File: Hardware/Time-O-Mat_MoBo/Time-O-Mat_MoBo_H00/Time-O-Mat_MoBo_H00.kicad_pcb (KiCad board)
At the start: 2 copper layers, 240 x 40 mm, 64 parts, among them J1 Conn_02x04_Odd_Even, J2 Conn_02x04_Odd_Even, J3 Conn_02x04_Odd_Even, J4 Conn_02x04_Odd_Even, J5 Conn_02x04_Odd_Even, J6 Conn_01x06_Male, J7 TYPE-C-31-M-12, J8 Conn_01x03, Q1 2N7002, Q2 S8050, Q3 S8050, Q4 2N7002, SW1 SW_SPST, SW2 SW_SPST, SW3 SW_SPST, U1 ESP32-WROOM-32D, U2 DS18B20, U3 DS1302ZN+, U4 AMS1117-3.3, U5 CH340G, Y1 Crystal_GND2

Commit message: HW updates
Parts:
- moved D1 164.9 mm to (214.4, 13.5), turned to -90 degrees
- moved J8 164.4 mm to (231.3, 11.0), turned to 90 degrees
- moved BZ1 159.0 mm to (205.4, 9.28), turned to -90 degrees
- moved Q1 140.4 mm to (196.6, 14.7)
- moved R9 133.9 mm to (22.9, 15.7)
- moved R6 130.2 mm to (13.8, 7.62), turned to -90 degrees
- moved R8 128.7 mm to (22.9, 14.2)
- moved C7 127.5 mm to (191.3, 4.95), turned to 90 degrees
- moved C13 124.2 mm to (33.0, 10.7)
- moved R7 119.9 mm to (11.7, 8.51), turned to 90 degrees
- moved C5 116.2 mm to (8.51, 24.0), turned to 90 degrees
- moved R1 115.5 mm to (193.7, 14.7), turned to -90 degrees
- moved R10 114.0 mm to (35.5, 17.0), turned to 180 degrees
- moved R3 112.3 mm to (190.8, 7.62)
- moved U2 112.2 mm to (196.5, 5.45), turned to 180 degrees
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- renumbered C5 to C4, C6 to C5, C4 to C6, SW2 to SW1, SW3 to SW2, SW1 to SW3
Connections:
- C4 pad 2: BUTTON2 -> BUTTON1
- C5 pad 2: BUTTON3 -> BUTTON2
- C6 pad 2: BUTTON1 -> BUTTON3
- SW1 pad 2: BUTTON2 -> BUTTON1
- SW2 pad 2: BUTTON3 -> BUTTON2
- SW3 pad 2: BUTTON1 -> BUTTON3
- Y1 pad 2: GND -> Net-(C9-Pad1)
- Y1 pad 3: Net-(C9-Pad1) -> GND
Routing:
- net +3V3: track 32.2 -> 269.6 mm, vias 0 -> 4
- net TEMPERATURE: track 0.00 -> 201.5 mm, vias 0 -> 8
- net BUZZER: track 0.00 -> 173.2 mm, vias 0 -> 6
- net CC1: track 0.00 -> 163.9 mm, vias 0 -> 6
- net CC2: track 0.00 -> 155.9 mm, vias 0 -> 4
- net IO: track 0.00 -> 150.3 mm, vias 0 -> 8
- net /USB+Power/ESP_RST: track 0.00 -> 109.1 mm
- net CE: track 0.00 -> 91.6 mm, vias 0 -> 4
- net LIGHT2: track 0.00 -> 90.0 mm, vias 0 -> 4
- net LIGHT1: track 0.00 -> 86.4 mm, vias 0 -> 4
- net SCLK: track 4.12 -> 84.6 mm, vias 2 -> 6
- net Net-(J1-Pad5): track 5.08 -> 74.3 mm
- net Net-(J4-Pad5): track 5.08 -> 71.5 mm
- net BUTTON1: track 0.00 -> 65.5 mm, vias 0 -> 2
- net BUTTON2: track 0.00 -> 59.7 mm, vias 0 -> 2
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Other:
- outline, holes or cut-outs redrawn

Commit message: HW updates
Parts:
- added G1: CoufalElektronika_logo, Time-O-Mat_Library:Coufal_elektronika_text_30x13mm, F.Cu at (180.5, 14.4)
- added G2: Vedatori_logo, Time-O-Mat_Library:Vedatori_copper_exposed_15mm, B.Cu at (175.4, 15.5)
- added G3: Vedatori_logo, Time-O-Mat_Library:Vedatori_15mm, F.Cu at (30.0, 31.8)
- added kibuzzard-61E8891A: G***, kibuzzard-61E8891A, F.Cu at (71.2, 9.53)
- added kibuzzard-61E88A0E: G***, kibuzzard-61E88A0E, B.Cu at (55.5, 17.4)
- moved H3 107.8 mm to (52.5, 5.50)
- moved H1 16.0 mm to (43.0, 36.0)
- moved H2 10.0 mm to (180.0, 24.0)
- moved H5 7.28 mm to (130.0, 24.0)
- moved H6 1.11 mm to (235.0, 24.0)
- moved H4 0.32 mm to (16.0, 36.0)
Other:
- board text added: "Electronics designed by: Marek Coufal Project design: Martin Ptáček Martin Coufal Aleš Kraml and other lovely and supportive members of the Vědátoři team."
- board text added: "Time-O-Mat_Mobo_H00"
- board text added: "{dblquote}The ultimate solution to time telling...{dblquote}"

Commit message: HW updates
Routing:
- net Net-(Q4-Pad2): track 15.6 -> 16.2 mm
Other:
- board text added: "+5V Data GND"
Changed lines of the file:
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@@
     (effects (font (size 3 3) (thickness 0.6) italic) (justify mirror))
+  )
+  (gr_text "+5V\nData\nGND" (at 233.68 15.367 90) (layer "F.SilkS")
+    (effects (font (size 1.4 1.4) (thickness 0.15)))
   )
   (gr_text "Electronics designed by: Marek Coufal\nProject design:\nMartin Ptáček\nMartin Coufal\nAleš Kraml\nand other lovely and supportive members of the Vědátoři team." (at 211.455 23.622) (layer "F.SilkS")
@@
   (segment (start 36.030497 27.559) (end 35.903497 27.686) (width 0.254) (layer "B.Cu") (net 57))
   (segment (start 36.030497 24.95498) (end 36.030497 27.559) (width 0.254) (layer "B.Cu") (net 57))
-  (segment (start 46.416 10.353) (end 48.372805 12.309805) (width 0.254) (layer "F.Cu") (net 63))
   (segment (start 49.313622 15.546315) (end 48.855875 15.088568) (width 0.254) (layer "F.Cu") (net 63))
   (segment (start 46.416 9.0655) (end 46.416 10.353) (width 0.254) (layer "F.Cu") (net 63))
   (segment (start 46.416 10.353) (end 46.416 11.178) (width 0.254) (layer "F.Cu") (net 63))
   (segment (start 51.357322 15.546315) (end 49.313622 15.546315) (width 0.254) (layer "F.Cu") (net 63))
-  (segment (start 48.372805 12.309805) (end 49.070836 12.309805) (width 0.254) (layer "F.Cu") (net 63))
   (segment (start 54.746 17.653) (end 53.464007 17.653) (width 0.254) (layer "F.Cu") (net 63))
+  (segment (start 46.416 11.428) (end 47.297805 12.309805) (width 0.254) (layer "F.Cu") (net 63))
+  (segment (start 47.297805 12.309805) (end 49.070836 12.309805) (width 0.254) (layer "F.Cu") (net 63))
   (segment (start 53.464007 17.653) (end 51.357322 15.546315) (width 0.254) (layer "F.Cu") (net 63))
   (segment (start 46.416 11.178) (end 46.291 11.303) (width 0.254) (layer "F.Cu") (net 63))
+  (segment (start 46.416 10.353) (end 46.416 11.428) (width 0.254) (layer "F.Cu") (net 63))
   (via (at 48.855875 15.088568) (size 0.6) (drill 0.3) (layers "F.Cu" "B.Cu") (net 63))
   (via (at 49.070836 12.309805) (size 0.6) (drill 0.3) (layers "F.Cu" "B.Cu") (net 63))

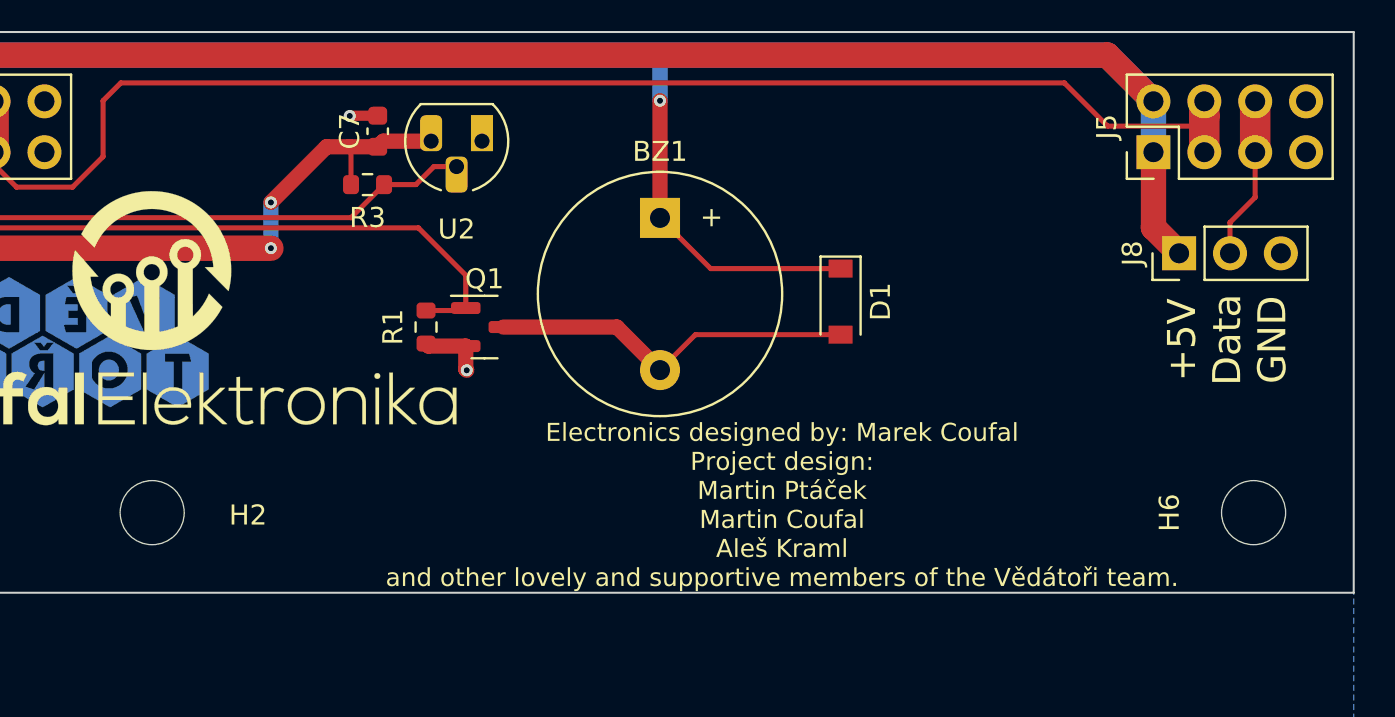
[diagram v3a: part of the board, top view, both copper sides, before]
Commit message: Exported up to date STEP models and manufacturing data
Exported up to date 3D models of all PCB parts.
Created new subpanels fot manufacturing to counteract duplicit designators on different boards.
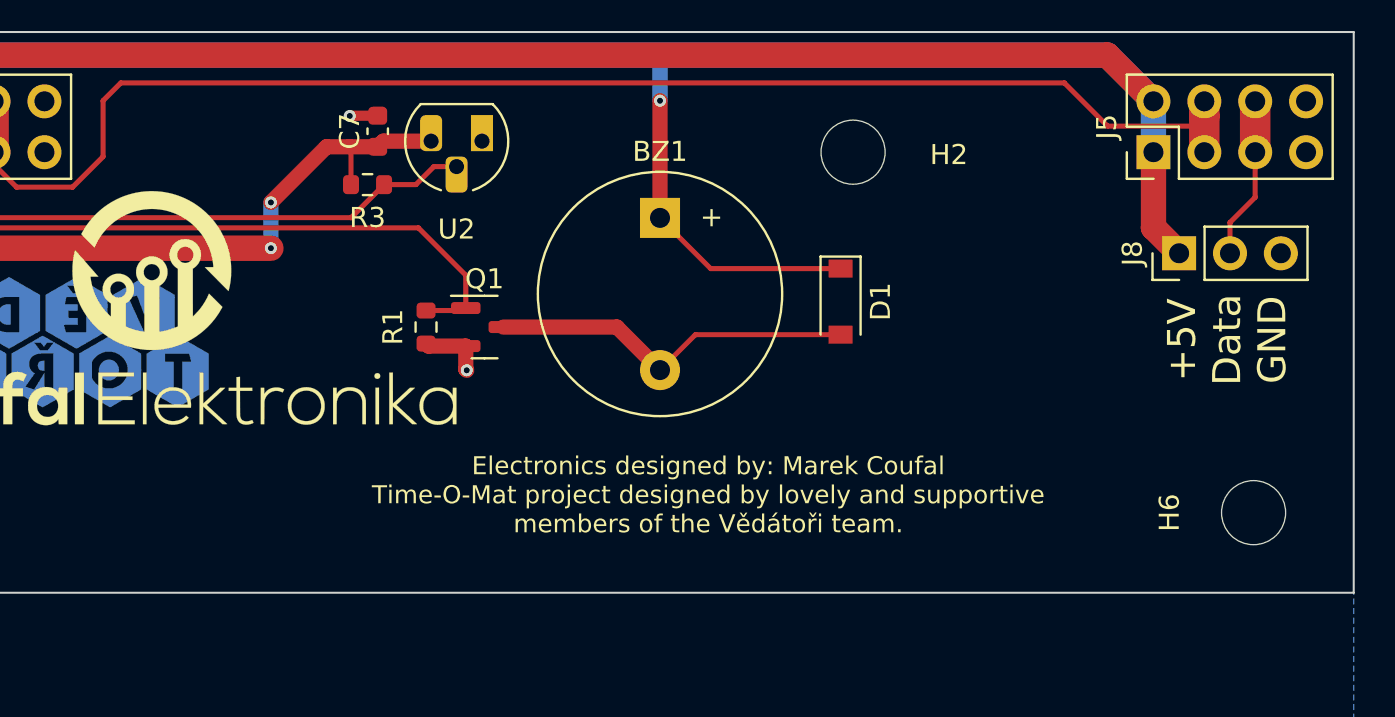
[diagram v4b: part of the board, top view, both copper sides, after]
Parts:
- J7: value TYPE-C-31-M-12 -> 918-418K2023S40001
- moved H2 39.4 mm to (215.0, 6.00)
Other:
- board text added: "Electronics designed by: Marek Coufal Time-O-Mat project designed by lovely and supportive members of the Vědátoři team."
- board text removed: "Electronics designed by: Marek Coufal Project design: Martin Ptáček Martin Coufal Aleš Kraml and other lovely and supportive members of the Vědátoři team."
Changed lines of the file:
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@@
     (descr "USB Type-C receptacle for USB 2.0 and PD, http://www.krhro.com/uploads/soft/180320/1-1P320120243.pdf")
     (tags "usb usb-c 2.0 pd")
-    (property "LCSC" "C165948")
+    (property "LCSC" "C167321")
     (property "Sheetfile" "USB+Power.kicad_sch")
     (property "Sheetname" "USB+Power")
@@
       (effects (font (size 1 1) (thickness 0.15)))
     )
-    (fp_text value "TYPE-C-31-M-12" (at 0 5.1 90) (layer "F.Fab")
+    (fp_text value "918-418K2023S40001" (at 0 5.1 90) (layer "F.Fab")
       (effects (font (size 1 1) (thickness 0.15)))
     )
@@
     (descr "SOIC, 8 Pin (JEDEC MS-012AA, https://www.analog.com/media/en/package-pcb-resources/package/pkg_pdf/soic_narrow-r/r_8.pdf), generated with kicad-footprint-generator ipc_gullwing_generator.py")
     (tags "SOIC SO")
+    (property "LCSC" "C910859")
     (property "Sheetfile" "Time-O-Mat_MoBo_H00.kicad_sch")
     (property "Sheetname" "")
@@
     (descr "Resistor SMD 0603 (1608 Metric), square (rectangular) end terminal, IPC_7351 nominal, (Body size source: IPC-SM-782 page 72, https://www.pcb-3d.com/wordpress/wp-content/uploads/ipc-sm-782a_amendment_1_and_2.pdf), generated with kicad-footprint-generator")
     (tags "resistor")
+    (property "LCSC" "C23162")
     (property "Sheetfile" "Time-O-Mat_MoBo_H00.kicad_sch")
     (property "Sheetname" "")
@@
     (descr "Capacitor SMD 0603 (1608 Metric), square (rectangular) end terminal, IPC_7351 nominal, (Body size source: IPC-SM-782 page 76, https://www.pcb-3d.com/wordpress/wp-content/uploads/ipc-sm-782a_amendment_1_and_2.pdf), generated with kicad-footprint-generator")
     (tags "capacitor")
+    (property "LCSC" "C37474")
     (property "Sheetfile" "Time-O-Mat_MoBo_H00.kicad_sch")
     (property "Sheetname" "")
@@
   )
   (footprint "MountingHole:MountingHole_3.2mm_M3" (layer "F.Cu")
-    (at 180 24)
+    (at 215 6)
     (descr "Mounting Hole 3.2mm, no annular, M3")
     (tags "mounting hole 3.2mm no annular m3")
@@
     (descr "Capacitor SMD 0603 (1608 Metric), square (rectangular) end terminal, IPC_7351 nominal, (Body size source: IPC-SM-782 page 76, https://www.pcb-3d.com/wordpress/wp-content/uploads/ipc-sm-782a_amendment_1_and_2.pdf), generated with kicad-footprint-generator")
     (tags "capacitor")
+    (property "LCSC" "C37474")
     (property "Sheetfile" "Time-O-Mat_MoBo_H00.kicad_sch")
     (property "Sheetname" "")
@@
     (effects (font (size 1.4 1.4) (thickness 0.15)))
   )
-  (gr_text "Electronics designed by: Marek Coufal\nProject design:\nMartin Ptáček\nMartin Coufal\nAleš Kraml\nand other lovely and supportive members of the Vědátoři team." (at 211.455 23.622) (layer "F.SilkS")
+  (gr_text "Electronics designed by: Marek Coufal\nTime-O-Mat project designed by lovely and supportive\nmembers of the Vědátoři team." (at 207.772 23.114) (layer "F.SilkS")
     (effects (font (size 0.9 0.9) (thickness 0.15)))
   )
